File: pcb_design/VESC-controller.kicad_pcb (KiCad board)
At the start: 2 copper layers, 160 x 92.5 mm, 135 parts, among them J1 GATE_DRIVER_CONN_U, J2 GATE_DRIVER_CONN_V, J3 GATE_DRIVER_CONN_W, P1 HALL/Encoder, P2 SWD, P3 PWR_COMM, P4 IN+, P5 IN-, U1 STM32F40X_LQFP64, U12 OPA2376AID, U15 OPA2376AID, U16 OPA2376AID, U17 LM2903-SO8, U2 ISO1050, U3 OPA2376AID, U4 LM2903-SO8, U5 7400-TSSOP, U6 SN74ALVC08PWR, U7 SN74ALVC08PWR, X1 MINI-USB-SHIELD-32005-201, X2 8MHz 10ppm

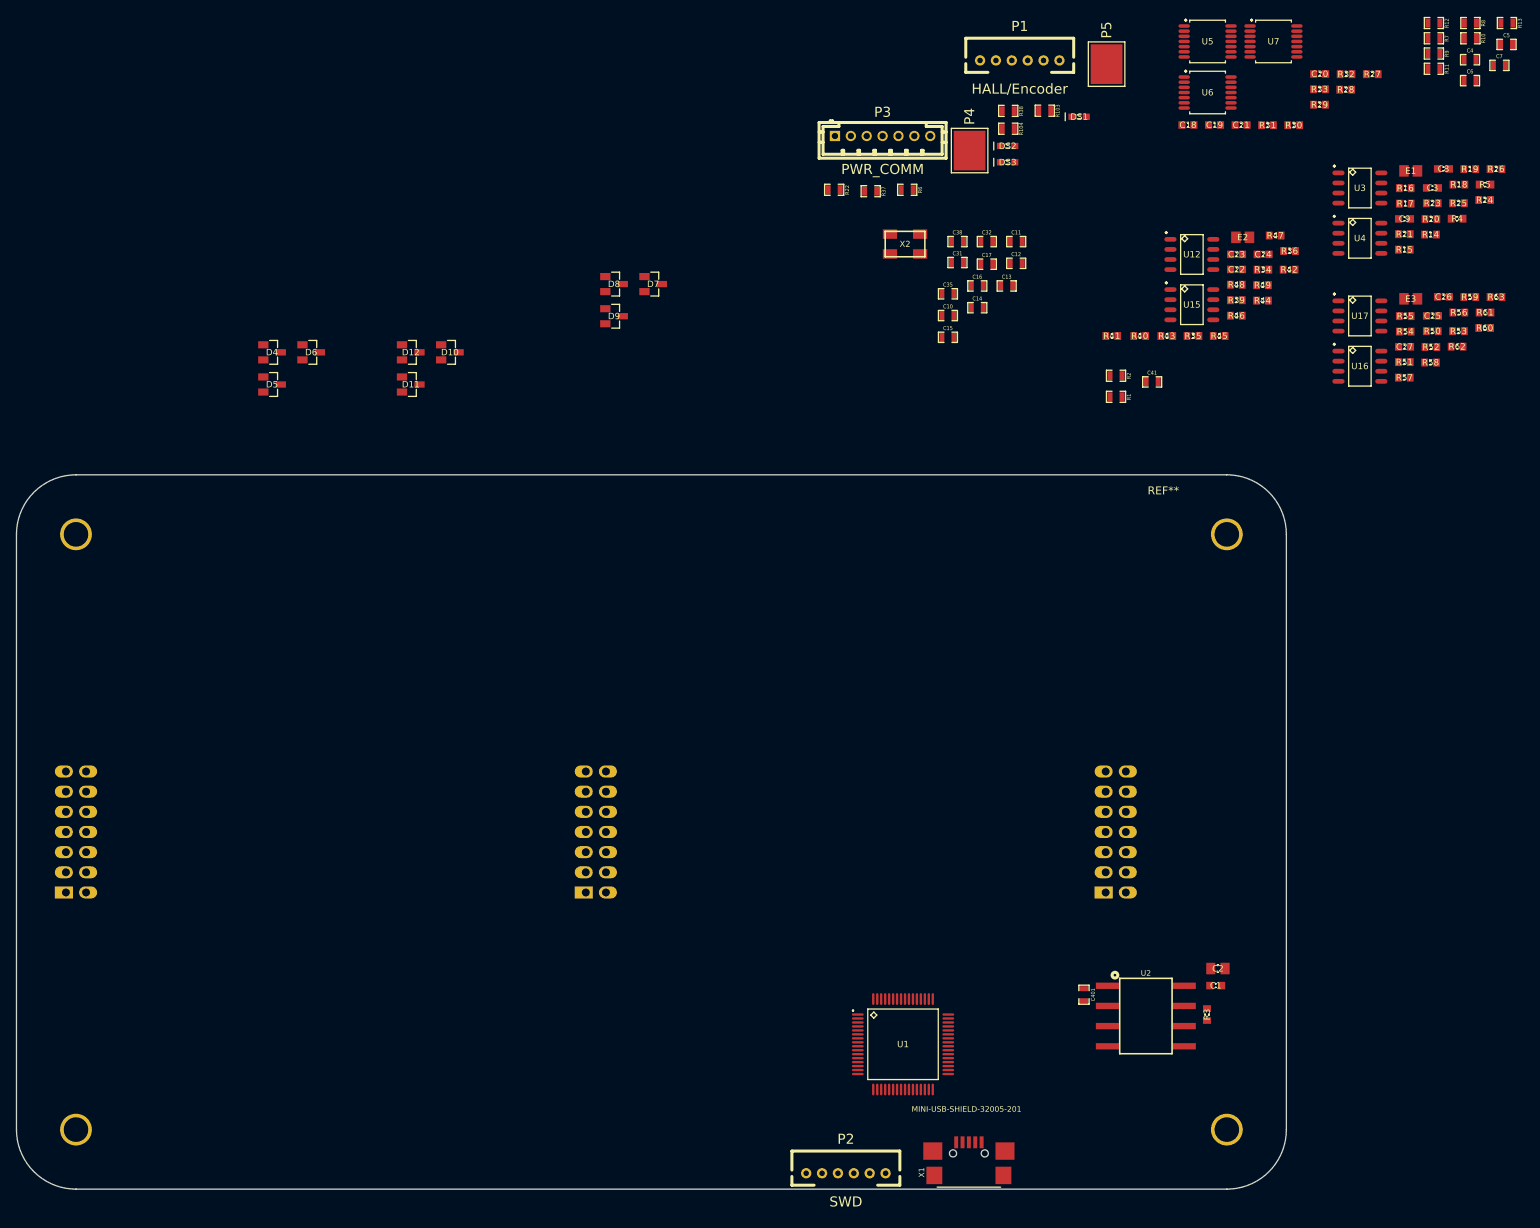
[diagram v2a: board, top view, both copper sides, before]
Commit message: Components placement, 3D models, updated some footprints to nominal IPC type
Signed-off-by: Marcos Chaparro <mchaparro@paltatech.com>
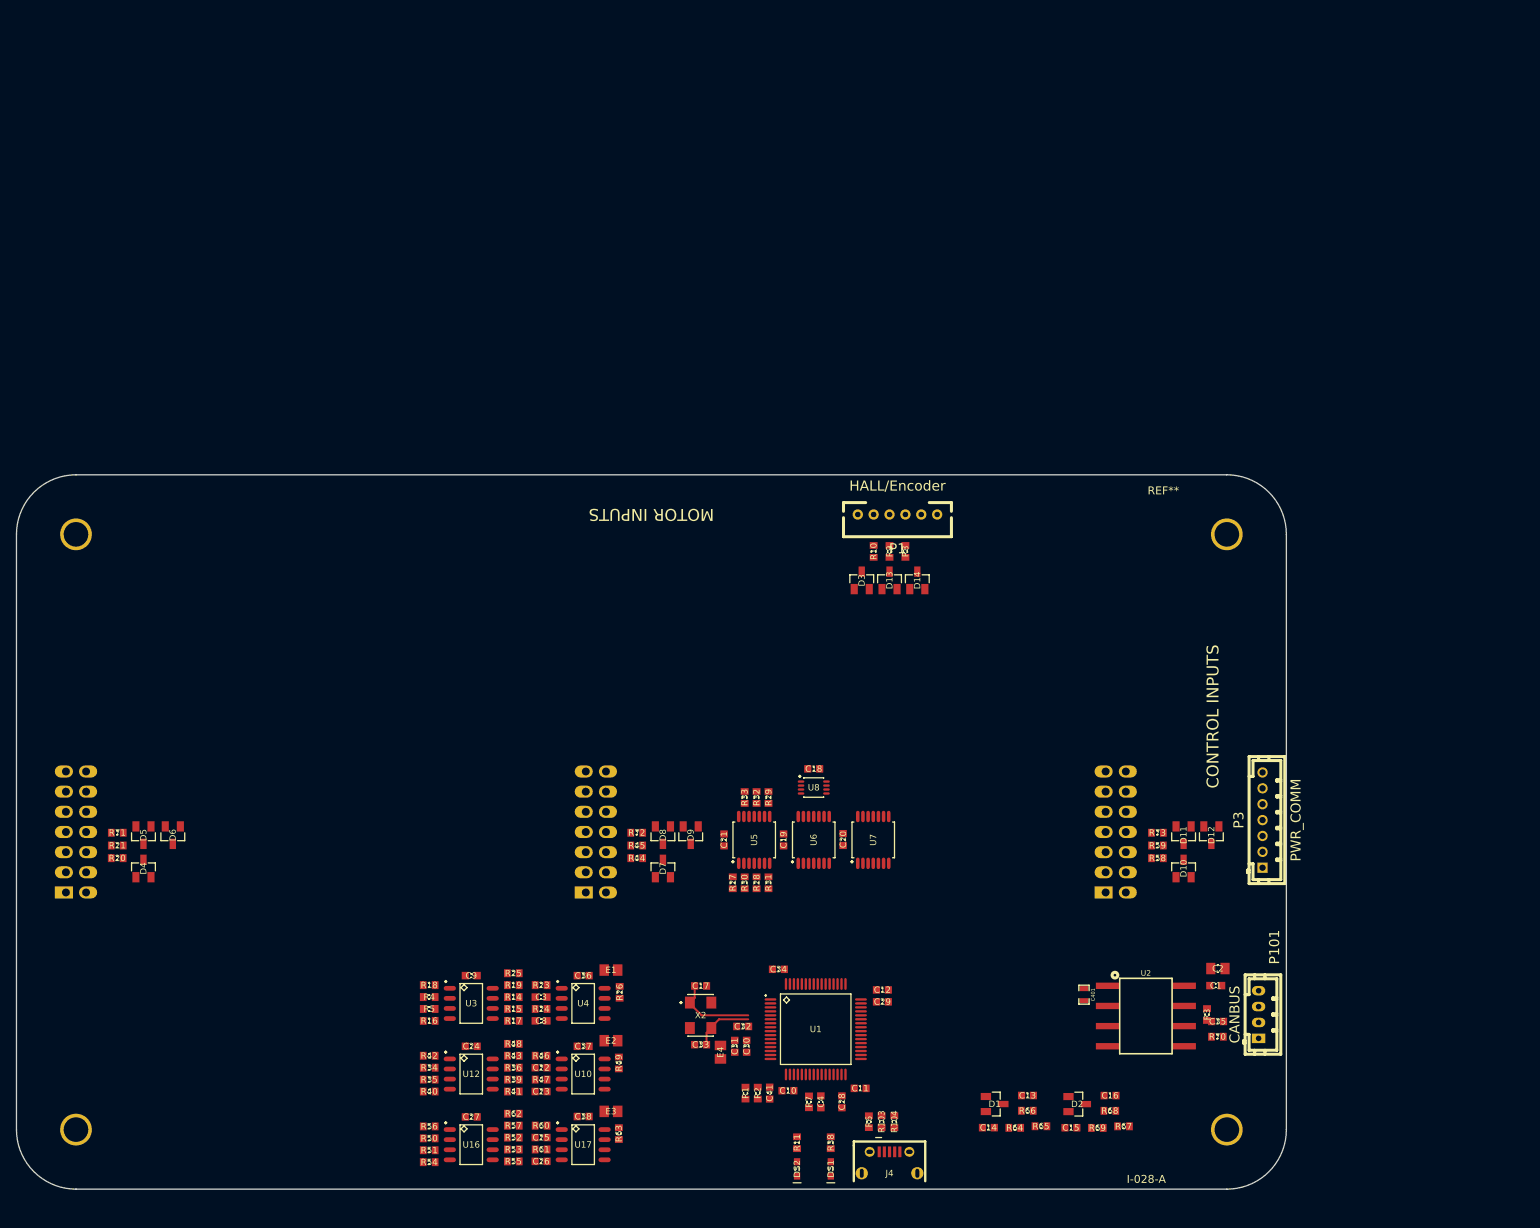
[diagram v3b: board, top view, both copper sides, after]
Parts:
- removed C5, C6, C7: 4n7, CRF1:SMD-0603_c
- removed DS3: GREEN, smd-semi:LED-0603
- removed P2: SWD, CRF1:MICRO_JST_6
- removed P4: IN+, CRF1:1PAD_4x5mm
- removed P5: IN-, CRF1:1PAD_4x5mm
- removed R12, R13, R22: 2k2, CRF1:SMD-0603_r
- removed R37: 100R, CRF1:SMD-0603_r
- removed U15: OPA2376AID, IPC7351-Nominal:SOIC127P600X175-8
- removed X1: MINI-USB-SHIELD-32005-201, paltatech:USB-UX60R-MB-5ST
- added C28: 2.2u, IPC7351-Nominal:CAPC1608X55, F.Cu at (24.0, 34.0)
- added C29: 2.2u, IPC7351-Nominal:CAPC1608X55, F.Cu at (29.1, 21.4)
- added C30: 100nF, IPC7351-Nominal:CAPC1608X55, F.Cu at (12.0, 27.0)
- added C33: 15p, IPC7351-Nominal:CAPC1608X55, F.Cu at (6.20, 26.8)
- added C34: 2.2u, IPC7351-Nominal:CAPC1608X55, F.Cu at (16.0, 17.3)
- added C36: 100nF, IPC7351-Nominal:CAPC1608X55, F.Cu at (-8.60, 18.1)
- added C37: 100nF, IPC7351-Nominal:CAPC1608X55, F.Cu at (-8.60, 27.0)
- added D1: BAT54S, smd-semi:SOT-23, F.Cu at (43.2, 34.3)
- added D13: BAT54S, smd-semi:SOT-23, F.Cu at (30.0, -31.7)
- added D14: BAT54S, smd-semi:SOT-23, F.Cu at (33.5, -31.7)
- added D2: BAT54S, smd-semi:SOT-23, F.Cu at (53.6, 34.3)
- added D3: BAT54S, smd-semi:SOT-23, F.Cu at (26.5, -31.7)
- added E4: BEAD-0805, IPC7351-Nominal:INDC2012X130, F.Cu at (8.70, 27.8)
- added J4: micro USB, conn-fci:CONN-10118194-0001LF-FCI, F.Cu at (30.0, 43.0)
- added P101: CANBUS, w_conn_jst-ph:b4b-ph-kl, F.Cu at (76.5, 23.0)
- added R64: 100R, IPC7351-Nominal:RESC1608X50, F.Cu at (45.8, 37.3)
- added R65: 5.2k, IPC7351-Nominal:RESC1608X50, F.Cu at (49.1, 37.1)
- added R66: 10k, IPC7351-Nominal:RESC1608X50, F.Cu at (47.4, 35.1)
- added R67: 100R, IPC7351-Nominal:RESC1608X50, F.Cu at (59.5, 37.1)
- added R68: 5.2k, IPC7351-Nominal:RESC1608X50, F.Cu at (57.8, 35.1)
- added R69: 10k, IPC7351-Nominal:RESC1608X50, F.Cu at (56.2, 37.3)
- added R70: 120R, IPC7351-Nominal:RESC1608X50, F.Cu at (71.3, 25.8)
- added R71: 22R, IPC7351-Nominal:RESC1608X50, F.Cu at (-67.3, 0.10)
- added R72: 22R, IPC7351-Nominal:RESC1608X50, F.Cu at (-1.85, 0.10)
- added R73: 22R, IPC7351-Nominal:RESC1608X50, F.Cu at (63.8, 0.10)
- added U10: LM2903-SO8, IPC7351-Nominal:SOIC127P600X175-8, F.Cu at (-8.60, 30.5)
- added U8: SN74AUP1G74, IPC7351-Nominal:SOP50P310X100-8, F.Cu at (20.4, -5.60)
- C10, C11, C12, C31, C32, C41: footprint CRF1:SMD-0603_c -> IPC7351-Nominal:CAPC1608X55
- C13, C14, C16: value 2.2u -> 1nF; footprint CRF1:SMD-0603_c -> IPC7351-Nominal:CAPC1608X55
- C15: value 15p -> 1nF; footprint CRF1:SMD-0603_c -> IPC7351-Nominal:CAPC1608X55
- C17: value 2.2u -> 15p; footprint CRF1:SMD-0603_c -> IPC7351-Nominal:CAPC1608X55
- C35: value 2.2u -> 100nF; footprint CRF1:SMD-0603_c -> IPC7351-Nominal:CAPC1608X55
- C38: value 15p -> 100nF; footprint CRF1:SMD-0603_c -> IPC7351-Nominal:CAPC1608X55
- C4: value 4n7 -> 4.7nF; footprint CRF1:SMD-0603_c -> IPC7351-Nominal:CAPC1608X55
- E1, E2, E3: value BEAD-0805 -> BEAD-220ohm@100khz
- R1, R10, R103, R104, R2, R38, R6, R7, R8, R9: footprint CRF1:SMD-0603_r -> IPC7351-Nominal:RESC1608X50
- R11: value 2k2 -> 100R; footprint CRF1:SMD-0603_r -> IPC7351-Nominal:RESC1608X50
- X2: value 8MHz 10ppm -> ABM3B - 8MHz; footprint CRF1:Crystal_5x3mm -> IPC7351-Nominal:OSCCC320X500X150
- moved R20 184.1 mm to (-67.3, 3.30)
- moved R21 179.5 mm to (-67.3, 1.70)
- moved R5 168.8 mm to (-28.0, 22.3), turned to 180 degrees
- moved R56 165.4 mm to (-28.0, 37.1), turned to 180 degrees
- moved R18 164.3 mm to (-28.0, 19.3), turned to 180 degrees
- moved R4 162.5 mm to (-28.0, 20.8), turned to 180 degrees
- moved R50 162.2 mm to (-28.0, 38.6), turned to 180 degrees
- moved R16 161.7 mm to (-28.0, 23.8), turned to 180 degrees
- moved R54 161.5 mm to (-28.0, 41.6), turned to 180 degrees
- moved R61 158.9 mm to (-13.9, 40.0)
- moved R19 158.4 mm to (-17.4, 19.3)
- moved R51 158.0 mm to (-28.0, 40.1), turned to 180 degrees
- moved R53 157.5 mm to (-17.4, 40.0)
- moved C26 157.4 mm to (-13.9, 41.5), turned to 180 degrees
- moved R11 157.3 mm to (18.4, 39.1), turned to 90 degrees
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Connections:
- net /MCU/ADC_TEMP renamed /STM32F4/ADC_TEMP
- net /MCU/DC_CAL renamed /STM32F4/PB12
- net /MCU/EN_GATE renamed /STM32F4/SPI3_SCK
- net /MCU/FAULT renamed /STM32F4/SPI3_MOSI
- net /MCU/SERVO renamed /STM32F4/~DRIVER_RESET
- net /MCU/USB_DM renamed /STM32F4/USB_DM
- net /MCU/USB_DP renamed /STM32F4/USB_DP
- net DRIVER_RESET renamed ~DRIVER_RESET
- net Net-(U1-Pad11) renamed /STM32F4/AN_IN
- net Net-(U1-Pad40) renamed /STM32F4/SPI3_CS
- net Net-(U1-Pad54) renamed /STM32F4/PD2
- net Net-(U1-Pad55) renamed /STM32F4/PB3
- net Net-(U1-Pad56) renamed /STM32F4/PB4
- C10 pad 1: GND -> VCC
- C10 pad 2: VCC -> GND
- C11 pad 1: GND -> VCC
- C11 pad 2: VCC -> GND
- C12 pad 1: GND -> VCC
- C12 pad 2: VCC -> GND
- C13 pad 1: GND -> Net-(C13-Pad1)
- C13 pad 2: VCC -> GND
- C14 pad 1: GND -> /Accel input conditioning/OUT
- C14 pad 2: VCC -> GND
- C16 pad 1: Net-(C16-Pad1) -> /STM32F4/ADC_15
- C17 pad 1: Net-(C17-Pad1) -> GND
- C17 pad 2: GND -> Net-(C17-Pad2)
- C31 pad 1: GND -> Net-(C30-Pad1)
- C31 pad 2: VCC -> GND
- C32 pad 1: GND -> /STM32F4/NRST
- C32 pad 2: NRST -> GND
- C35 pad 1: GND -> /Isolated CAN/GND_CAN
- C35 pad 2: VCC -> Net-(C35-Pad2)
- C38 pad 1: Net-(C38-Pad1) -> /conditioning W/3.3V_AN
- C4 pad 1: GND -> /Filters/TEMP_IN
- C4 pad 2: /Filters/TEMP_IN -> GND
- D12 pad 3: /conditioning W/Power_good -> Net-(D12-Pad3)
- D6 pad 3: /conditioning U/Power_good -> Net-(D6-Pad3)
- D9 pad 3: /conditioning V/Power_good -> Net-(D9-Pad3)
- J1 pad 12: FAULT -> ~FAULT
- J2 pad 12: FAULT -> ~FAULT
- J3 pad 12: FAULT -> ~FAULT
- R10 pad 1: /Filters/HALL3_IN -> /Filters/HALL3_OUT
- R10 pad 2: /Filters/HALL3_OUT -> /Filters/HALL3_IN
- R11 pad 1: /Filters/HALL3_IN -> Net-(DS2-Pad2)
- R11 pad 2: VCC -> /STM32F4/LED_GREEN
- R27 pad 1: /Supervisor/PWM_UT -> /STM32F4/PWM_UT
- R28 pad 1: /Supervisor/PWM_VT -> /STM32F4/PWM_VT
- R29 pad 1: /Supervisor/PWM_WT -> /STM32F4/PWM_WT
- R3 pad 1: /Isolated CAN/CANH -> Net-(C35-Pad2)
- R30 pad 1: /Supervisor/PWM_UB -> /STM32F4/PWM_UB
- R31 pad 1: /Supervisor/PWM_VB -> /STM32F4/PWM_VB
- R32 pad 1: /Supervisor/PWM_WB -> /STM32F4/PWM_WB
- R38 pad 2: /MCU/LED_RED -> /STM32F4/LED_RED
- R8 pad 1: /Filters/HALL1_IN -> /Filters/HALL1_OUT
- R8 pad 2: /Filters/HALL1_OUT -> /Filters/HALL1_IN
- R9 pad 1: /Filters/HALL2_IN -> /Filters/HALL2_OUT
- R9 pad 2: /Filters/HALL2_OUT -> /Filters/HALL2_IN
- U1 pad 10: /MCU/AN_IN -> /conditioning W/I_phase
- U1 pad 13: VCC -> Net-(C30-Pad1)
- U1 pad 14: /MCU/SENS3 -> /conditioning U/V_phase
- U1 pad 15: /MCU/SENS2 -> /conditioning V/V_phase
- U1 pad 16: /MCU/SENS1 -> /conditioning W/V_phase
- U1 pad 24: /MCU/LED_GREEN -> /Filters/TEMP_IN
- U1 pad 25: /MCU/LED_RED -> /STM32F4/ADC_15
- U1 pad 26: /MCU/BR_SO2 -> /STM32F4/LED_GREEN
- U1 pad 27: /MCU/BR_SO1 -> /STM32F4/LED_RED
- U1 pad 31: Net-(C16-Pad1) -> Net-(C28-Pad2)
- U1 pad 34: /MCU/L3 -> /STM32F4/PWM_UB
- U1 pad 35: /MCU/L2 -> /STM32F4/PWM_VB
- U1 pad 36: /MCU/L1 -> /STM32F4/PWM_WB
- U1 pad 37: /TX_SDA -> /Filters/HALL1_OUT
- U1 pad 38: /RX_SCL_MOSI -> /Filters/HALL2_OUT
- U1 pad 39: Net-(U1-Pad39) -> /Filters/HALL3_OUT
- U1 pad 41: /MCU/H3 -> /STM32F4/PWM_UT
- U1 pad 42: /MCU/H2 -> /STM32F4/PWM_VT
- U1 pad 43: /MCU/H1 -> /STM32F4/PWM_WT
- U1 pad 46: SWDIO -> /STM32F4/SWDIO
- U1 pad 47: Net-(C17-Pad1) -> Net-(C29-Pad2)
- U1 pad 49: SWCLK -> /STM32F4/SWCLK
- U1 pad 5: Net-(C15-Pad1) -> Net-(C17-Pad2)
- U1 pad 52: /Filters/HALL3_OUT -> /STM32F4/SPI3_MISO
- U1 pad 58: /Filters/HALL1_OUT -> -VEE_ctrl
- U1 pad 59: /Filters/HALL2_OUT -> FAULT
- U1 pad 6: Net-(C38-Pad1) -> Net-(C33-Pad2)
- U1 pad 7: NRST -> /STM32F4/NRST
- U1 pad 8: /Filters/TEMP_IN -> /conditioning U/I_phase
- U1 pad 9: Net-(U1-Pad9) -> /conditioning V/I_phase
- U12 pad 8: /conditioning W/3.3V_AN -> /conditioning V/3.3V_AN
- U16 pad 4: (no net) -> GND
- U16 pad 8: (no net) -> /conditioning W/3.3V_AN
- U17 pad 4: (no net) -> GND
- U17 pad 5: (no net) -> Net-(U17-Pad5)
- U17 pad 6: (no net) -> Net-(U17-Pad6)
- U17 pad 7: (no net) -> Net-(U17-Pad7)
- U17 pad 8: (no net) -> /conditioning W/3.3V_AN
- U4 pad 4: (no net) -> GND
- U4 pad 5: Net-(C23-Pad1) -> Net-(U4-Pad5)
- U4 pad 6: Net-(C22-Pad1) -> Net-(U4-Pad6)
- U4 pad 7: /conditioning U/OC_Fault -> Net-(U4-Pad7)
- U4 pad 8: (no net) -> /conditioning U/3.3V_AN
- U5 pad 1: /Supervisor/PWM_UT -> /STM32F4/PWM_UT
- U5 pad 10: /Supervisor/PWM_WB -> /STM32F4/PWM_WB
- U5 pad 14: (no net) -> VCC
- U5 pad 2: /Supervisor/PWM_UB -> /STM32F4/PWM_UB
- U5 pad 4: /Supervisor/PWM_VT -> /STM32F4/PWM_VT
- U5 pad 5: /Supervisor/PWM_VB -> /STM32F4/PWM_VB
- U5 pad 7: (no net) -> GND
- U5 pad 9: /Supervisor/PWM_WT -> /STM32F4/PWM_WT
- U6 pad 1: /Supervisor/PWM_UT -> /STM32F4/PWM_UT
- U6 pad 13: /Supervisor/PWM_VB -> /STM32F4/PWM_VB
- U6 pad 5: /Supervisor/PWM_UB -> /STM32F4/PWM_UB
- U6 pad 9: /Supervisor/PWM_VT -> /STM32F4/PWM_VT
- U7 pad 1: /Supervisor/PWM_WT -> /STM32F4/PWM_WT
- U7 pad 10: /Supervisor/~FAULT -> FAULT
- U7 pad 5: /Supervisor/PWM_WB -> /STM32F4/PWM_WB
- X2 pad 1: Net-(C15-Pad1) -> Net-(C17-Pad2)
- X2 pad 2: Net-(C38-Pad1) -> GND
- X2 pad 3: GND -> Net-(C33-Pad2)
- X2 pad 4: (no net) -> GND
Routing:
- net Net-(C17-Pad2): track 0.00 -> 10.4 mm
- net Net-(C33-Pad2): track 0.00 -> 7.53 mm
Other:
- board text added: "CONTROL INPUTS"
- board text added: "I-028-A"
- board text added: "MOTOR INPUTS"

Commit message: Added terminal blocks and power supplies
Signed-off-by: Marcos Chaparro <mchaparro@paltatech.com>
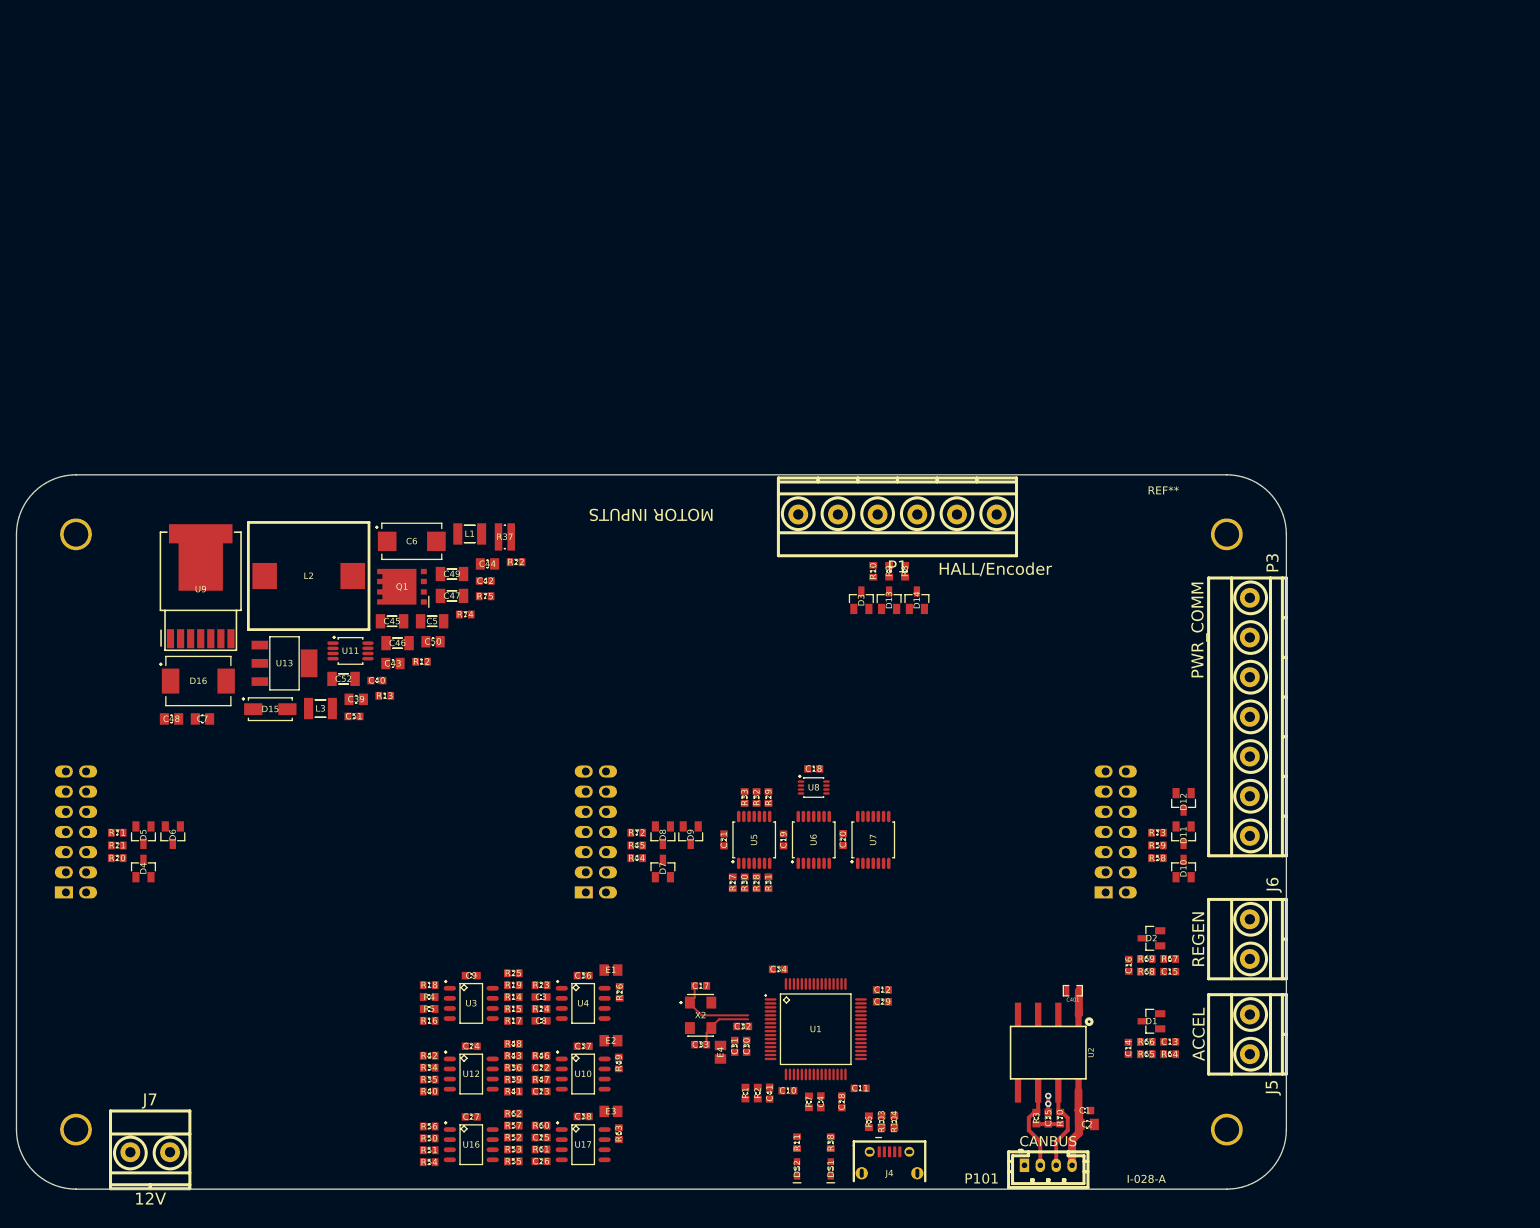
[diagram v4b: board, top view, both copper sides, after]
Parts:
- added C39: 1uF 50v, IPC7351-Nominal:CAPC2012X70, F.Cu at (-37.2, -16.7)
- added C40: 180nF, IPC7351-Nominal:CAPC1608X55, F.Cu at (-34.6, -19.1)
- added C42: 180nF, IPC7351-Nominal:CAPC1608X55, F.Cu at (-20.9, -31.6)
- added C43: 1uF 50v, IPC7351-Nominal:CAPC2012X70, F.Cu at (-32.6, -21.2)
- added C44: 680pF, IPC7351-Nominal:CAPC2012X70, F.Cu at (-20.7, -33.8)
- added C45: 2.2uF 50v, IPC7351-Nominal:CAPC3216X70, F.Cu at (-32.7, -26.5)
- added C46: 22uF 10v, IPC7351-Nominal:CAPC3216X70, F.Cu at (-32.0, -23.8)
- added C47: 22uF 10v, IPC7351-Nominal:CAPC3216X70, F.Cu at (-25.1, -29.7)
- added C48: 22uF, IPC7351-Nominal:CAPC2012X70, F.Cu at (-60.5, -14.2)
- added C49: 22uF 10v, IPC7351-Nominal:CAPC3216X70, F.Cu at (-25.1, -32.5)
- added C5: 10uF 50v, IPC7351-Nominal:CAPC3216X70, F.Cu at (-27.6, -26.5)
- added C50: 22uF, IPC7351-Nominal:CAPC2012X70, F.Cu at (-27.5, -24.0)
- added C51: 100nF, IPC7351-Nominal:CAPC1608X55, F.Cu at (-37.5, -14.6)
- added C52: 22uF 10v, IPC7351-Nominal:CAPC3216X70, F.Cu at (-38.8, -19.3)
- added C6: 4.7uF 50v, IPC7351-Nominal:CAPMP7343X310, F.Cu at (-30.2, -36.6)
- added C7: 750pF, IPC7351-Nominal:CAPC2012X70, F.Cu at (-56.6, -14.2)
- added D15: SS16, IPC7351-Nominal:DIOM5326X292, F.Cu at (-48.0, -15.5)
- added D16: 30BQ100TR, IPC7351-Nominal:DIOM7959X265, F.Cu at (-57.1, -19.0)
- added J5: ACCEL, w_conn_mkds:mkds_1,5-2, F.Cu at (75.4, 25.5)
- added J6: REGEN, w_conn_mkds:mkds_1,5-2, F.Cu at (75.4, 13.5)
- added J7: 12V, w_conn_mkds:mkds_1,5-2, F.Cu at (-63.1, 40.4)
- added L1: L-1210, IPC7351-Nominal:INDC3225X135, F.Cu at (-22.9, -37.5)
- added L2: 27uH, manuf:BOURNS-SRP1238A, F.Cu at (-43.2, -32.2)
- added L3: L-1210, IPC7351-Nominal:INDC3225X135, F.Cu at (-41.7, -15.5)
- added Q1: BSC340N08, manuf:TEXAS-Q5A, F.Cu at (-31.4, -30.9)
- added R12: 1.78k, IPC7351-Nominal:RESC1608X50, F.Cu at (-29.0, -21.4)
- added R13: 33.2k, IPC7351-Nominal:RESC1608X50, F.Cu at (-33.6, -17.1)
- added R22: 100R, IPC7351-Nominal:RESC1608X50, F.Cu at (-17.1, -34.0)
- added R37: 18mOhm, IPC7351-Nominal:CAPC1632X76, F.Cu at (-18.5, -37.2)
- added R74: 180k, IPC7351-Nominal:RESC1608X50, F.Cu at (-23.5, -27.4)
- added R75: 10k, IPC7351-Nominal:RESC1608X50, F.Cu at (-21.0, -29.7)
- added U11: LM3488, IPC7351-Nominal:SOP65P490X109-8, F.Cu at (-37.9, -22.8)
- added U13: LM1117IMP-v.v, smd-semi:SOT-223, F.Cu at (-46.2, -21.2)
- added U9: LM22676QTJ-5.0, manuf:TO-263-7-TEXAS, F.Cu at (-56.8, -30.6)
- P1: footprint CRF1:MICRO_JST_6 -> w_conn_mkds:mkds_1,5-6
- P3: footprint CRF1:b7b-ph-kl -> w_conn_mkds:mkds_1,5-7
- moved P101 32.6 mm to (50.0, 42.0), turned to 0 degrees
- moved C2 25.6 mm to (54.9, 36.9)
- moved R3 25.2 mm to (48.5, 36.0), turned to 90 degrees
- moved C35 24.6 mm to (50.0, 36.0), turned to 270 degrees
- moved C15 23.3 mm to (65.3, 17.6)
- moved D2 22.9 mm to (63.0, 13.4), turned to 180 degrees
- moved C1 22.8 mm to (54.6, 35.1)
- moved D1 22.3 mm to (63.0, 23.9), turned to 180 degrees
- moved R70 22.3 mm to (51.5, 36.0), turned to 270 degrees
- moved R69 22.2 mm to (62.4, 16.0), turned to 180 degrees
- moved R67 21.9 mm to (65.3, 16.0)
- moved R64 21.6 mm to (65.3, 28.0)
- moved C14 20.3 mm to (60.1, 27.2), turned to 90 degrees
- moved C13 19.1 mm to (65.3, 26.4)
- moved R68 18.1 mm to (62.4, 17.6)
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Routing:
- net /Isolated CAN/5v_CAN: track 0.00 -> 11.6 mm
- net /Isolated CAN/CANL: track 0.00 -> 10.6 mm
- net /Isolated CAN/CANH: track 0.00 -> 10.6 mm
- net VCC: track 0.00 -> 3.02 mm
- net Net-(C35-Pad2): track 0.00 -> 3.00 mm
- net /Isolated CAN/GND_CAN: track 0.00 -> 2.05 mm, vias 0 -> 2
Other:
- board text removed: "CONTROL INPUTS"
